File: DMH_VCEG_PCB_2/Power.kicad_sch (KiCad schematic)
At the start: 60 parts, among them J100 IDC_02x08, U1 TL074, U10 TL074, U11 4001, U12 40106, U13 CD4066BE, U14 TL074, U15 TL074, U16 TL074, U17 TL074, U18 TL074, U19 4001, U2 4001, U20 4001, U21 TL072, U3 40106, U4 CD4066BE, U5 TL074, U6 TL074, U7 TL074, U8 TL074, U9 TL074

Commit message: Added Output attenuation circuit
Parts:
- removed U21: TL072, Package_DIP:DIP-8_W7.62mm_Socket, symbol Amplifier_Operational:TL072
- added U21: TL074, Package_DIP:DIP-14_W7.62mm_Socket, symbol Amplifier_Operational:TL074
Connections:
- net +12V: now also U21.4 (V+)
- net -12V: now also U21.11 (V-)
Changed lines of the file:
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@@
+	)
+	(symbol
+		(lib_id "Amplifier_Operational:TL074")
+		(at 154.94 171.45 0)
+		(unit 5)
+		(exclude_from_sim no)
+		(in_bom yes)
+		(on_board yes)
+		(dnp no)
+		(fields_autoplaced yes)
+		(property "Reference" "U21"
+			(at 153.67 170.1799 0)
+			(effects
+				(font
+					(size 1.27 1.27)
+				)
+				(justify left)
+			)
+		)
+		(property "Value" "TL074"
+			(at 153.67 172.7199 0)
+			(effects
+				(font
+					(size 1.27 1.27)
+				)
+				(justify left)
+			)
+		)
+		(property "Footprint" "Package_DIP:DIP-14_W7.62mm_Socket"
+			(at 153.67 168.91 0)
+			(effects
+				(font
+					(size 1.27 1.27)
+				)
+				(hide yes)
+			)
+		)
+		(property "Datasheet" "http://www.ti.com/lit/ds/symlink/tl071.pdf"
+			(at 156.21 166.37 0)
+			(effects
+				(font
+					(size 1.27 1.27)
+				)
+				(hide yes)
+			)
+		)
+		(property "Description" "Quad Low-Noise JFET-Input Operational Amplifiers, DIP-14/SOIC-14"
+			(at 154.94 171.45 0)
+			(effects
+				(font
+					(size 1.27 1.27)
+				)
+				(hide yes)
+			)
+		)
+		(pin "8"
+		)
+		(pin "5"
+		)
+		(pin "12"
+		)
+		(pin "4"
+		)
+		(pin "7"
+		)
+		(pin "3"
+		)
+		(pin "6"
+		)
+		(pin "9"
+		)
+		(pin "11"
+		)
+		(pin "10"
+		)
+		(pin "14"
+		)
+		(pin "13"
+		)
+		(pin "1"
+		)
+		(pin "2"
+		)
+		(instances
+			(project ""
+				(path "/58f4306d-5387-4983-bb08-41a2313fd315/0cdf34b2-39cd-4d9e-981a-97cd34791509"
+					(reference "U21")
+					(unit 5)
+				)
+			)
+		)
 	)
 	(symbol
@@
 				)
 			)
-		)
-	)
-	(symbol
-		(lib_id "Amplifier_Operational:TL072")
-		(at 154.94 171.45 0)
-		(unit 3)
-		(exclude_from_sim no)
-		(in_bom yes)
-		(on_board yes)
-		(dnp no)
-		(fields_autoplaced yes)
-		(property "Reference" "U21"
-			(at 153.67 170.1799 0)
-			(effects
-				(font
-					(size 1.27 1.27)
-				)
-				(justify left)
-			)
-		)
-		(property "Value" "TL072"
-			(at 153.67 172.7199 0)
-			(effects
-				(font
-					(size 1.27 1.27)
-				)
-				(justify left)
-			)
-		)
-		(property "Footprint" "Package_DIP:DIP-8_W7.62mm_Socket"
-			(at 154.94 171.45 0)
-			(effects
-				(font
-					(size 1.27 1.27)
-				)
-				(hide yes)
-			)
-		)
-		(property "Datasheet" "http://www.ti.com/lit/ds/symlink/tl071.pdf"
-			(at 154.94 171.45 0)
-			(effects
-				(font
-					(size 1.27 1.27)
-				)
-				(hide yes)
-			)
-		)
-		(property "Description" "Dual Low-Noise JFET-Input Operational Amplifiers, DIP-8/SOIC-8"
-			(at 154.94 171.45 0)
-			(effects
-				(font
-					(size 1.27 1.27)
-				)
-				(hide yes)
-			)
-		)
-		(pin "4"
-		)
-		(pin "2"
-		)
-		(pin "7"
-		)
-		(pin "8"
-		)
-		(pin "1"
-		)
-		(pin "6"
-		)
-		(pin "3"
-		)
-		(pin "5"
-		)
-		(instances
-			(project ""
-				(path "/58f4306d-5387-4983-bb08-41a2313fd315/0cdf34b2-39cd-4d9e-981a-97cd34791509"
-					(reference "U21")
-					(unit 3)
-				)
-			)

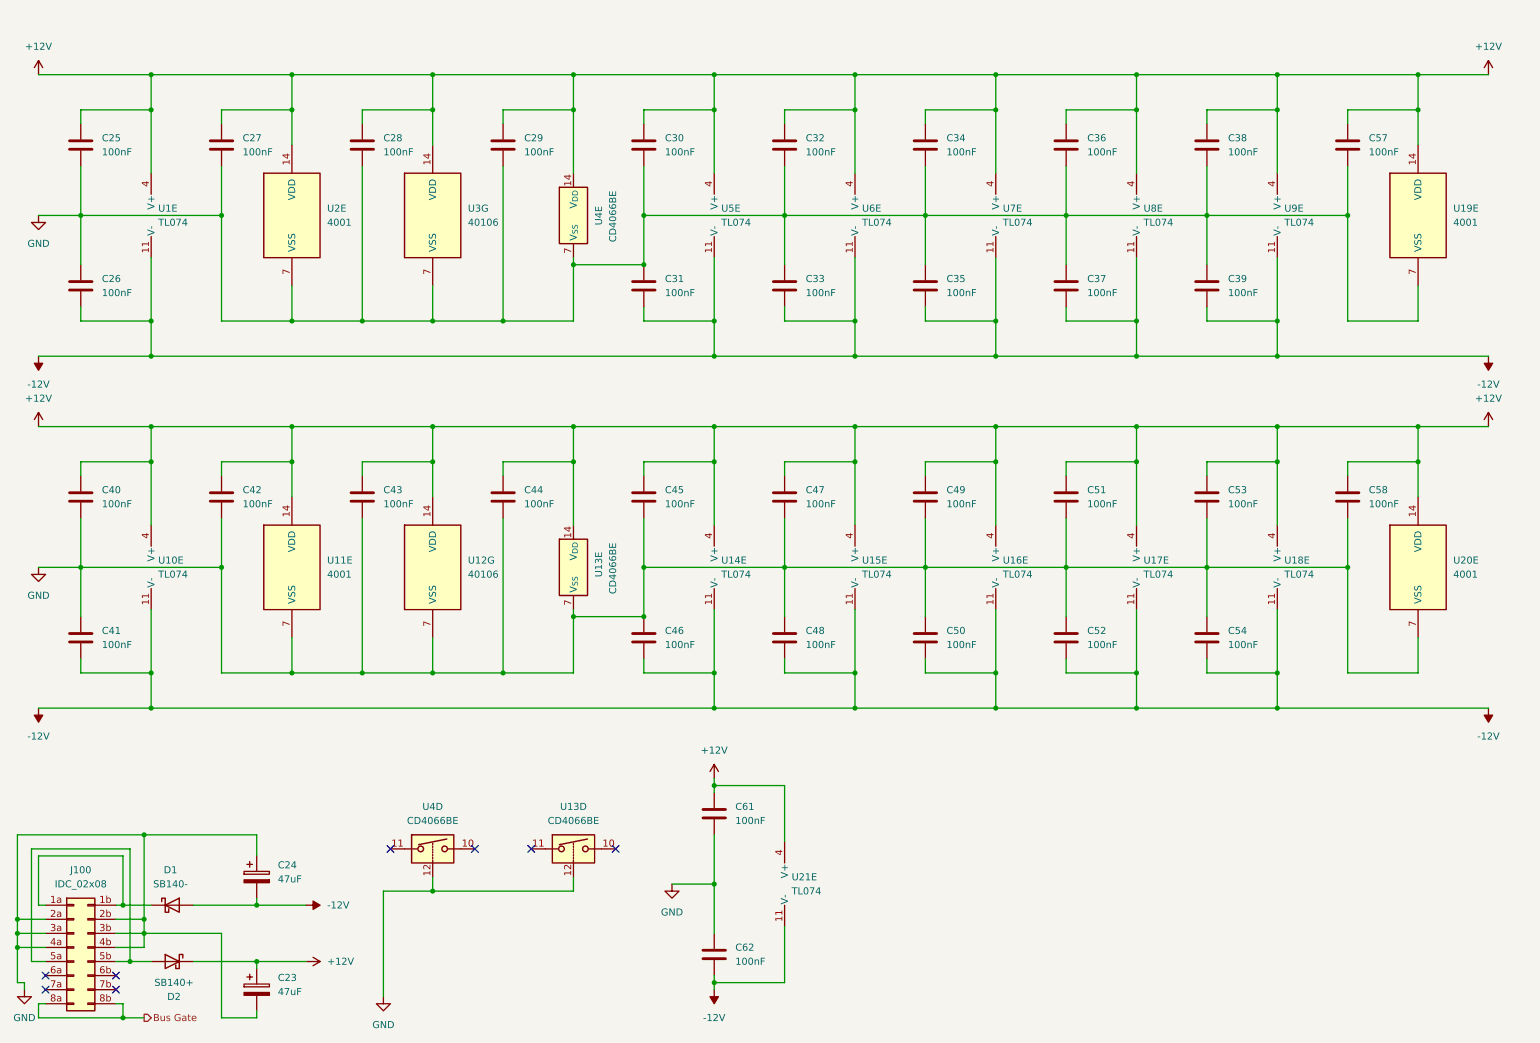
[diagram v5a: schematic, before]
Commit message: Synced PCB 2 project with PCB 1
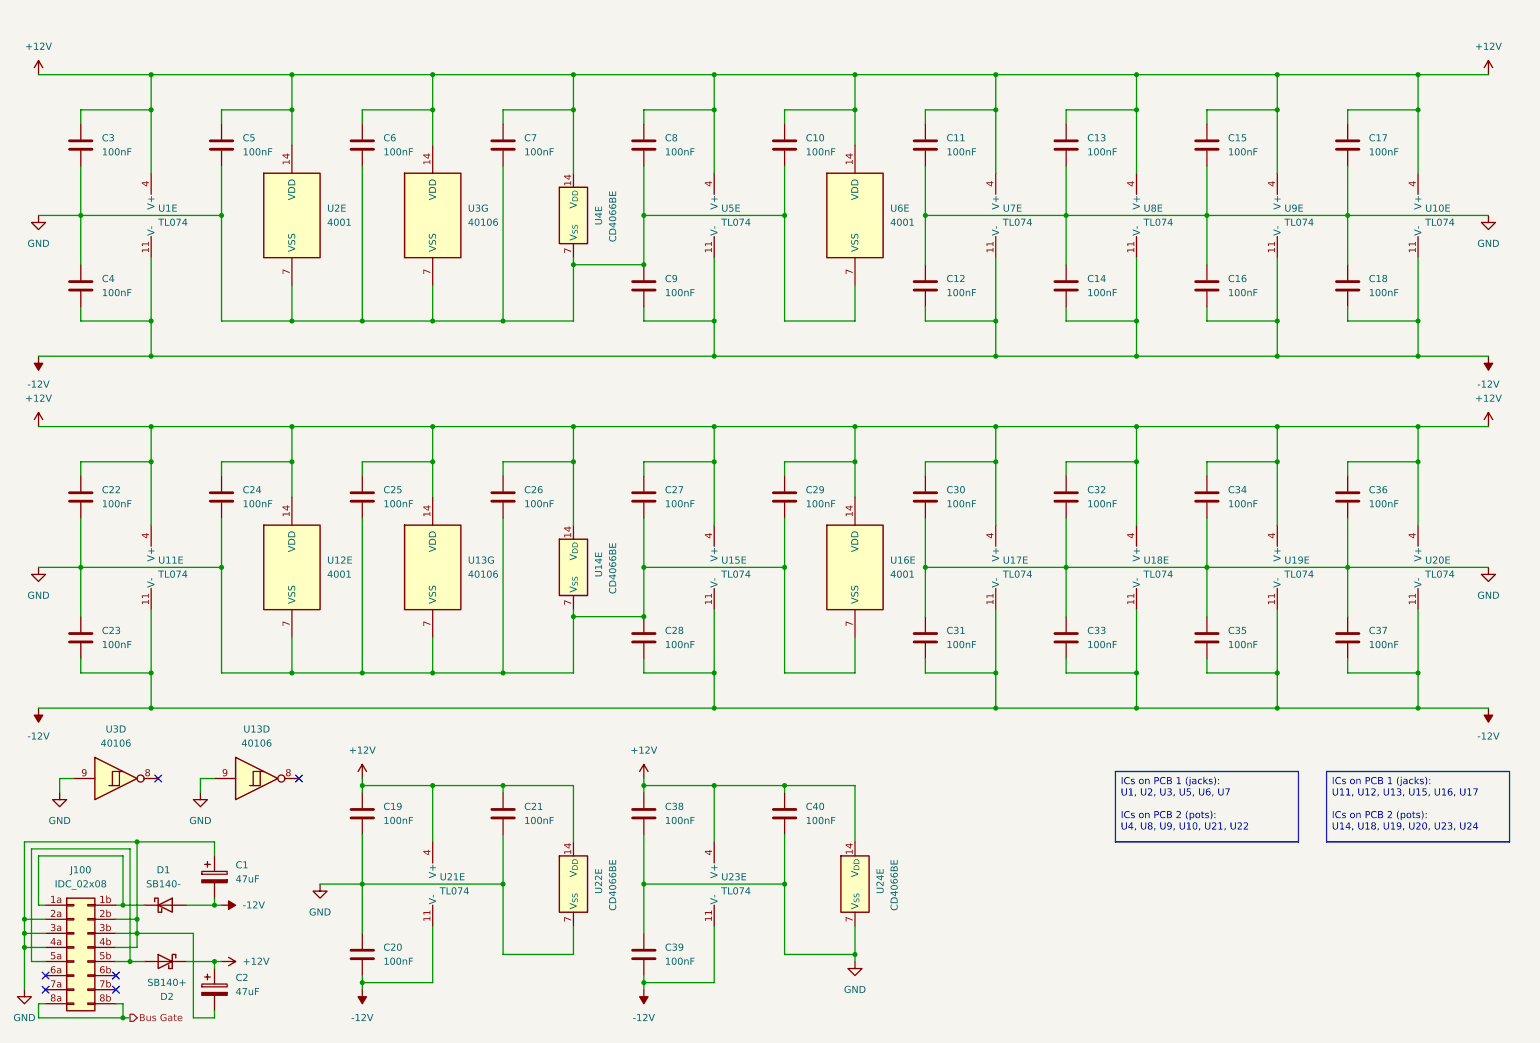
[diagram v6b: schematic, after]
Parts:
- removed C47, C48, C58: 100nF, Capacitor_THT:C_Disc_D4.3mm_W1.9mm_P5.00mm, symbol Device:C
- removed unit 4 of U13
- removed U15, U6: TL074, Package_DIP:DIP-14_W7.62mm_Socket, symbol Amplifier_Operational:TL074
- removed unit 4 of U4
- added C19, C20, C21, C29, C36, C37, C40: 100nF, Capacitor_THT:C_Disc_D4.3mm_W1.9mm_P5.00mm, symbol Device:C
- added U10, U20, U23: TL074, Package_DIP:DIP-14_W7.62mm_Socket, symbol Amplifier_Operational:TL074
- added unit 4 of U13
- added U22, U24: CD4066BE, Package_DIP:DIP-14_W7.62mm, symbol Analog_Switch:CD4066BE
- added unit 4 of U3
- C1: renamed from C24; footprint Capacitor_THT:CP_Radial_D5.0mm_P2.00mm -> Capacitor_THT:CP_Radial_D4.0mm_P1.50mm
- C2: renamed from C23; footprint Capacitor_THT:CP_Radial_D5.0mm_P2.00mm -> Capacitor_THT:CP_Radial_D4.0mm_P1.50mm
- renumbered C57 to C10, C34 to C11, C35 to C12, C36 to C13, C37 to C14, C38 to C15, C39 to C16, C32 to C17, C33 to C18, C40 to C22, C41 to C23, C42 to C24, C43 to C25, C44 to C26, C45 to C27, C46 to C28, C25 to C3, C49 to C30, C50 to C31, C51 to C32, C52 to C33, C53 to C34, C54 to C35, C61 to C38, C62 to C39, C26 to C4, C27 to C5, C28 to C6, C29 to C7, C30 to C8, C31 to C9, U10 to U11, U11 to U12, U12 to U13, U13 to U14, U14 to U15, U20 to U16, U16 to U17, U17 to U18, U18 to U19, U19 to U6
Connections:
- net +12V: now also C19.1, C21.1, C29.1, C36.1, C40.1, U10.4 (V+), U20.4 (V+), U22.14 (V_{DD}), U23.4 (V+), U24.14 (V_{DD})
- net -12V: now also C20.2, C37.2, U10.11 (V-), U20.11 (V-), U23.11 (V-)
- net GND: now also C19.2, C20.1, C21.2, C29.2, C36.2, C37.1, C40.2, U13.9, U22.7 (V_{SS}), U24.7 (V_{SS}), U3.9
- no-connect marks 8 -> 6
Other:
- moved on the sheet: C1, C10, C17, C18, C2, C38, C39, D1, D2, U16E, U6E

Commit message: Started placement on PCB 2
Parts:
- C1, C2: footprint Capacitor_THT:CP_Radial_D4.0mm_P1.50mm -> Capacitor_THT:CP_Radial_D5.0mm_P2.00mm
- U14, U22, U24, U4: footprint Package_DIP:DIP-14_W7.62mm -> Package_DIP:DIP-14_W7.62mm_Socket
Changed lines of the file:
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@@
 			)
 		)
-		(property "Footprint" "Capacitor_THT:CP_Radial_D4.0mm_P1.50mm"
+		(property "Footprint" "Capacitor_THT:CP_Radial_D5.0mm_P2.00mm"
 			(at 50.4952 173.99 0)
 			(effects
@@
 		(exclude_from_sim no)
 		(in_bom yes)
-		(on_board no)
+		(on_board yes)
 		(dnp no)
 		(fields_autoplaced yes)
@@
 		(exclude_from_sim no)
 		(in_bom yes)
-		(on_board no)
+		(on_board yes)
 		(dnp no)
 		(fields_autoplaced yes)
@@
 			)
 		)
-		(property "Footprint" "Package_DIP:DIP-14_W7.62mm"
+		(property "Footprint" "Package_DIP:DIP-14_W7.62mm_Socket"
 			(at 165.1 173.99 0)
 			(effects
@@
 			)
 		)
-		(property "Footprint" "Package_DIP:DIP-14_W7.62mm"
+		(property "Footprint" "Package_DIP:DIP-14_W7.62mm_Socket"
 			(at 114.3 116.84 0)
 			(effects
@@
 		(exclude_from_sim no)
 		(in_bom yes)
-		(on_board no)
+		(on_board yes)
 		(dnp no)
 		(fields_autoplaced yes)
@@
 			)
 		)
-		(property "Footprint" "Package_DIP:DIP-14_W7.62mm"
+		(property "Footprint" "Package_DIP:DIP-14_W7.62mm_Socket"
 			(at 114.3 173.99 0)
 			(effects
@@
 			)
 		)
-		(property "Footprint" "Package_DIP:DIP-14_W7.62mm"
+		(property "Footprint" "Package_DIP:DIP-14_W7.62mm_Socket"
 			(at 114.3 53.34 0)
 			(effects
@@
 			)
 		)
-		(property "Footprint" "Capacitor_THT:CP_Radial_D4.0mm_P1.50mm"
+		(property "Footprint" "Capacitor_THT:CP_Radial_D5.0mm_P2.00mm"
 			(at 50.4952 194.31 0)
 			(effects
@@
 		(exclude_from_sim no)
 		(in_bom yes)
-		(on_board no)
+		(on_board yes)
 		(dnp no)
 		(fields_autoplaced yes)
@@
 		(exclude_from_sim no)
 		(in_bom yes)
-		(on_board no)
+		(on_board yes)
 		(dnp no)
 		(fields_autoplaced yes)
@@
 		(exclude_from_sim no)
 		(in_bom yes)
-		(on_board no)
+		(on_board yes)
 		(dnp no)
 		(fields_autoplaced yes)

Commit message: Synced changes to PCB 2
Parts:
- removed unit 4 of U13
- removed unit 4 of U3
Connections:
- no-connect marks 6 -> 4
